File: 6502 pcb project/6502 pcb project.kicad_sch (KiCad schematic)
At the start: 4 parts

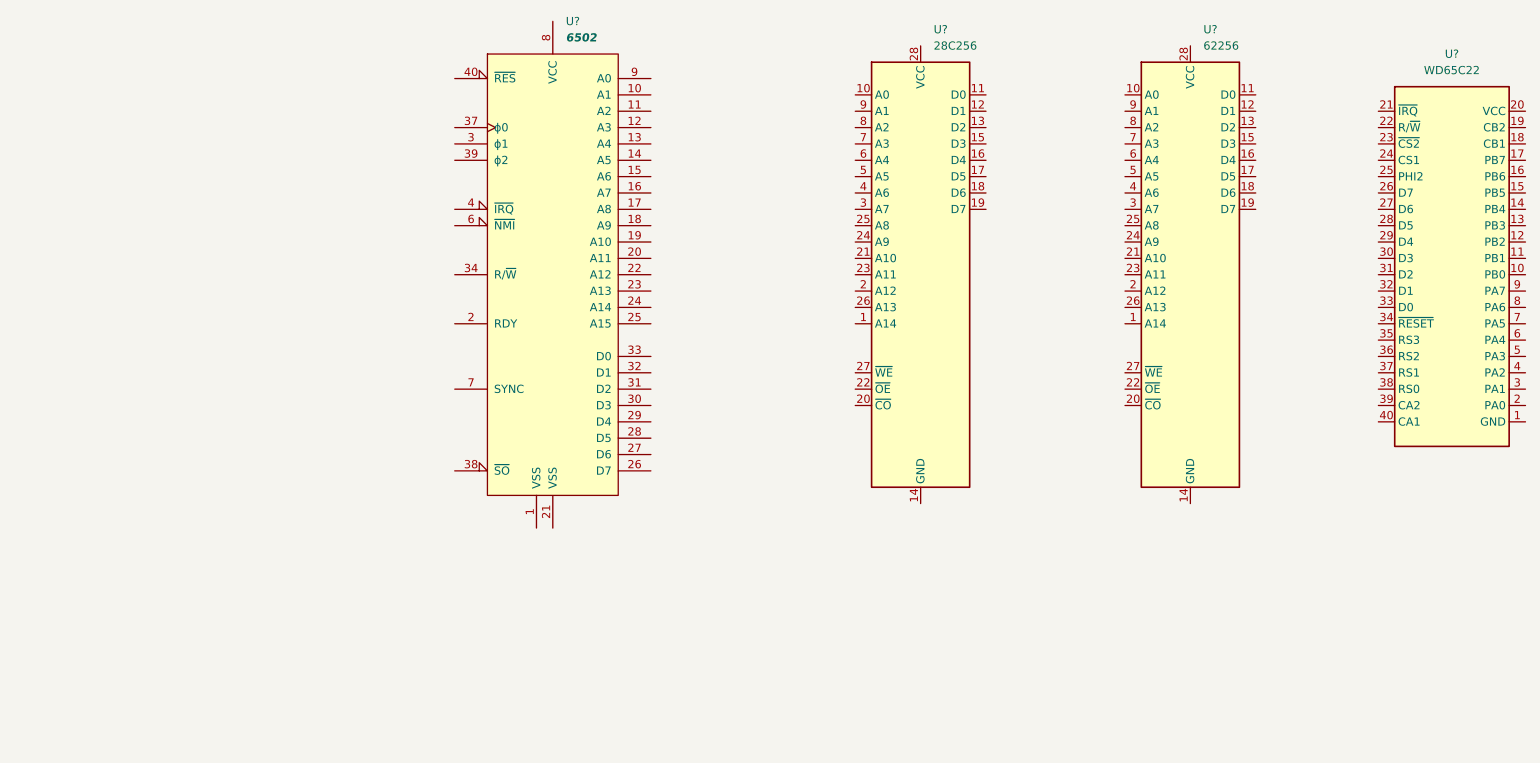
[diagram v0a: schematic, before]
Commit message: added bus lines for address and data
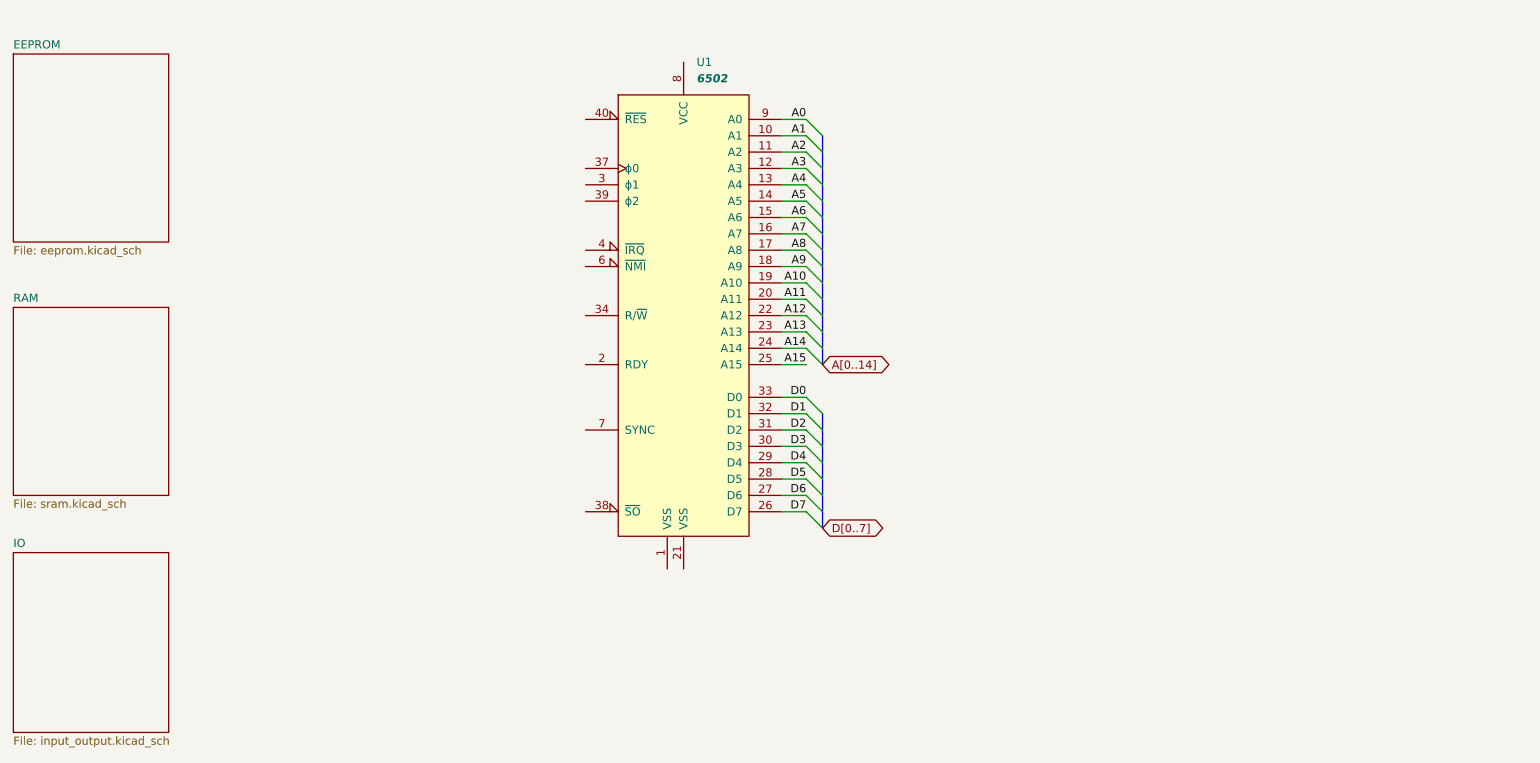
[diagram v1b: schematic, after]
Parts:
- removed U?: 28C256, symbol micro_controller:28C256
- removed U?: WD65C22, symbol micro_controller:WD65C22
- removed U?: 62256, symbol micro_controller:62256
- gave numbers to parts that had none: 1
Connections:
- net A1: now reaches U1.10 (A1)
- net A2: now reaches U1.11 (A2)
- net A3: now reaches U1.12 (A3)
- net A4: now reaches U1.13 (A4)
- net A5: now reaches U1.14 (A5)
- net A6: now reaches U1.15 (A6)
- net A7: now reaches U1.16 (A7)
- net A8: now reaches U1.17 (A8)
- net A9: now reaches U1.18 (A9)
- net A10: now reaches U1.19 (A10)
- net A11: now reaches U1.20 (A11)
- net A12: now reaches U1.22 (A12)
- net A13: now reaches U1.23 (A13)
- net A14: now reaches U1.24 (A14)
- net A15: now reaches U1.25 (A15)
- net D7: now reaches U1.26 (D7)
- net D6: now reaches U1.27 (D6)
- net D5: now reaches U1.28 (D5)
- net D4: now reaches U1.29 (D4)
- net D3: now reaches U1.30 (D3)
- net D2: now reaches U1.31 (D2)
- net D1: now reaches U1.32 (D1)
- net D0: now reaches U1.33 (D0)
- net A0: now reaches U1.9 (A0)
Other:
- added sheet EEPROM (eeprom.kicad_sch)
- added sheet IO (input_output.kicad_sch)
- added sheet RAM (sram.kicad_sch)
- moved on the sheet: U1
